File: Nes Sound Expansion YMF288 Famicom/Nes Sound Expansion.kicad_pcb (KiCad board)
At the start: 2 copper layers, 67 x 99 mm, 39 parts, among them J1 OUT, J2 EXP 1-30, J3 EXP 1-30, J4 31-60, J8 EXP 25-48, J9 EXP 1-24, U1 74LS139, U10 74LS257, U2 74LS132, U3 LM321, U6 74LS174, U7 74LS174, U8 74LS257, U9 74LS257, X1 CXO_DIP8

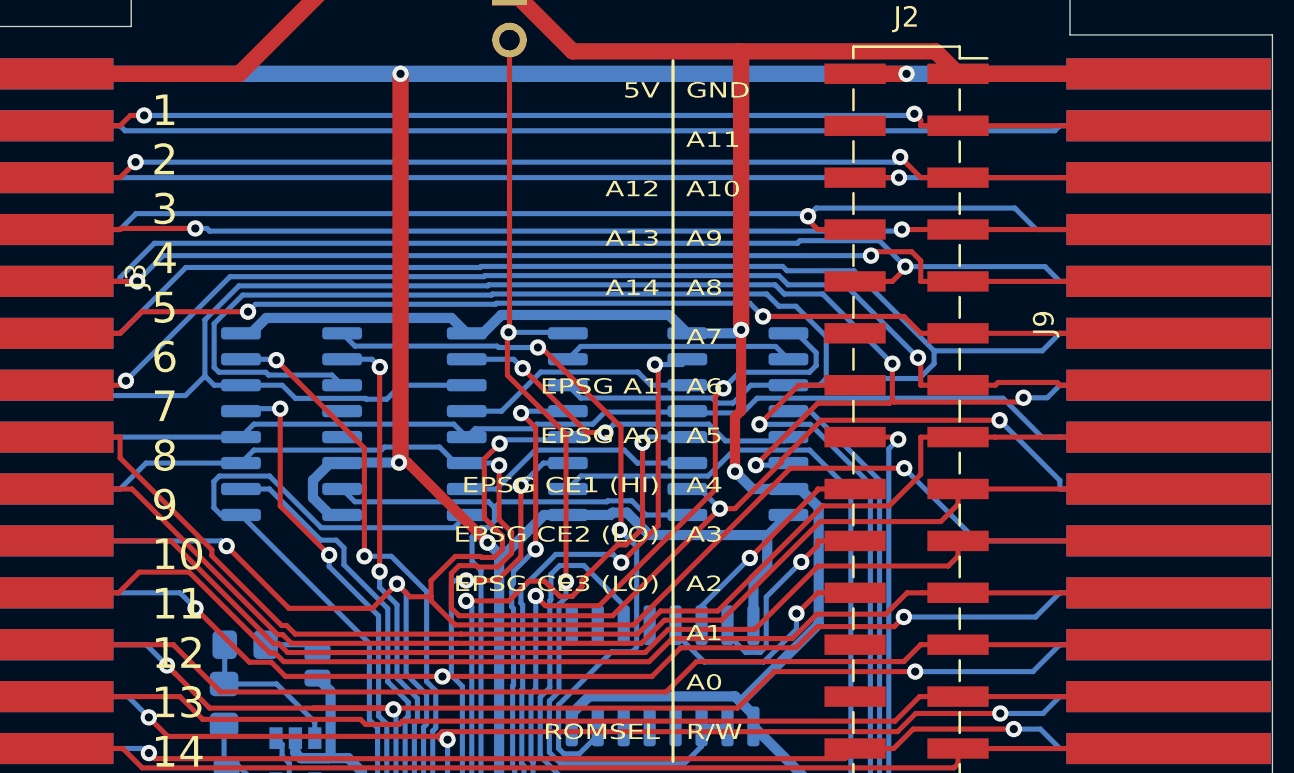
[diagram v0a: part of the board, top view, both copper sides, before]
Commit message: Added M2 to the addressing circuit and famicom daughterboard connector
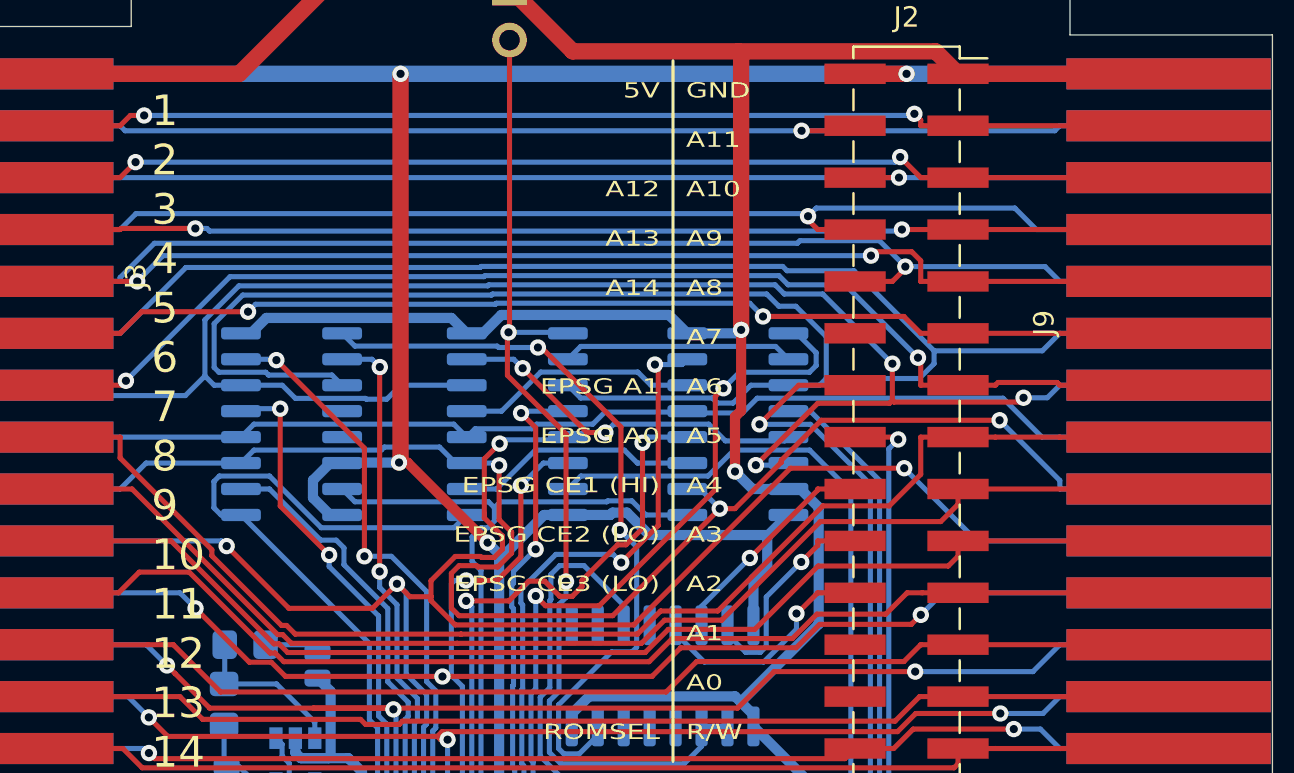
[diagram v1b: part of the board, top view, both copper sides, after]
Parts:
- removed G***: LOGO, Nes Sound Expansion OPNA:EPSM Logo
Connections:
- J2 pad 4: (no net) -> M2
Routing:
- net M2: track 56.8 -> 59.6 mm, vias 0 -> 1
